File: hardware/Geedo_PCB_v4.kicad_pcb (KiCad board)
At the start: 2 copper layers, 29.5 x 51.5 mm, 23 parts, among them J1 USB-C, J2 BATTERY, J3 OLED, SW1 MAIN_BTN, SW2 BOOT_BTN, SW3 RESET_BTN, U1 MCP73831, U2 AMS1117-3.3, U3 ESP32-C3-MINI-1

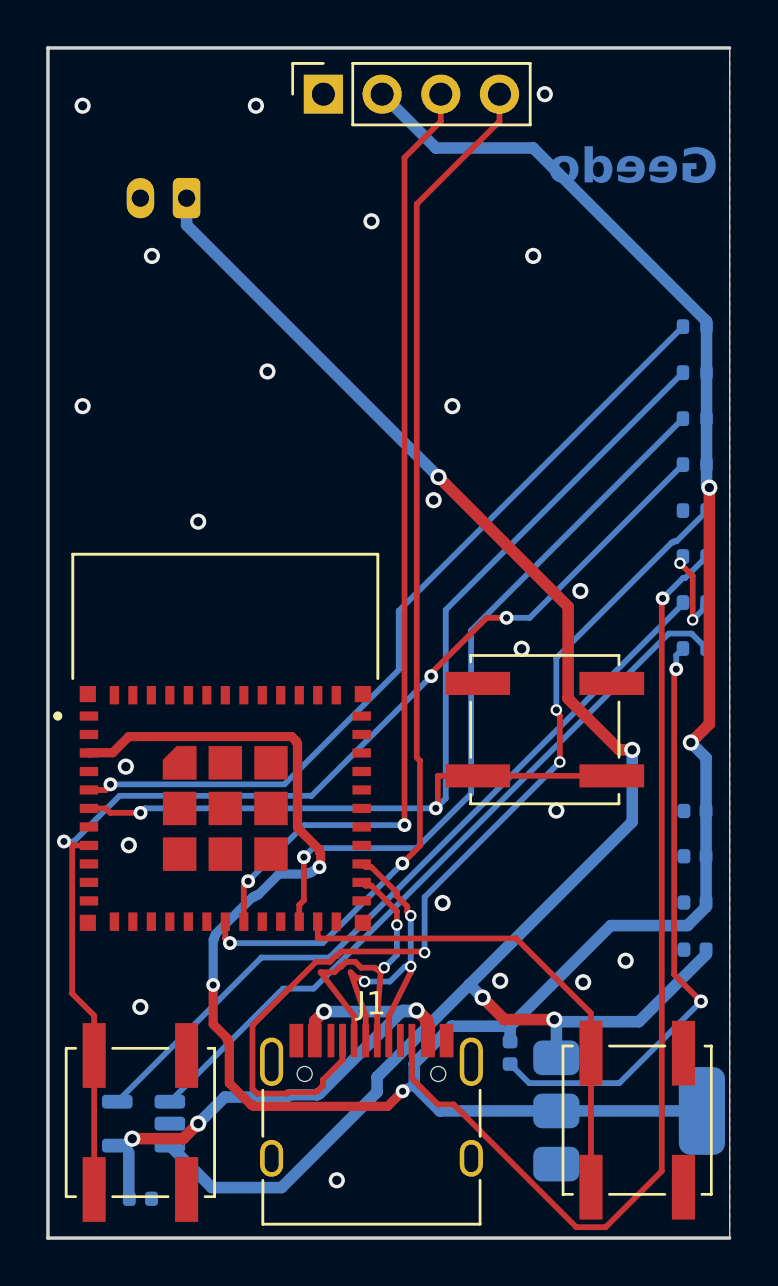
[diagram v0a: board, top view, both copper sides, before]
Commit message: hardware: replace AMS1117 with MCP1826S low-dropout regulator
The AMS1117 needs ~1.1 V of headroom, so on a LiPo it only holds 3.3 V near
full charge: at 3.7 V nominal the rail sits around 3.0 V, and an ESP32-C3's
300-400 mA WiFi transmit bursts widen the dropout further. The board would
have reset during WiFi at half battery - fatal for a robot that depends on
WiFi for updates and events.

MCP1826S-3302 drops 0.25 V and holds 3.3 V down to ~3.55 V of battery, using
the same SOT-223 footprint. It is not pin-compatible (AMS1117 is GND/Vout/Vin
with the tab on Vout; MCP1826S is Vin/GND/Vout with the tab on GND), so U2's
pads were remapped and VBAT/3V3 re-routed around it. The schematic symbol was
renumbered rather than redrawn, leaving every existing wire in place. The tab
now bonds to the ground pour, which also helps thermally.

Added C6, 1 uF on the back 2 mm from the output pin, as a local output
capacitor - C2's 10 uF sits 9 mm away. Its first position overlapped a 3V3
track and a VBAT via; the clearance audit caught both and it was moved to a
spot verified clear of every pad, track and via, with a gap even to same-net
pads.

Verified: schematic-to-board netlist 29/29 correct, every net except the
unfilled GND pour resolves to one island, and clearance is unchanged at the
9 pre-existing violations with none introduced.

Co-Authored-By: Claude Opus 5 <noreply@anthropic.com>
Claude-Session: https://claude.ai/code/session_011AnT632DFTLYxaJBrifUnG
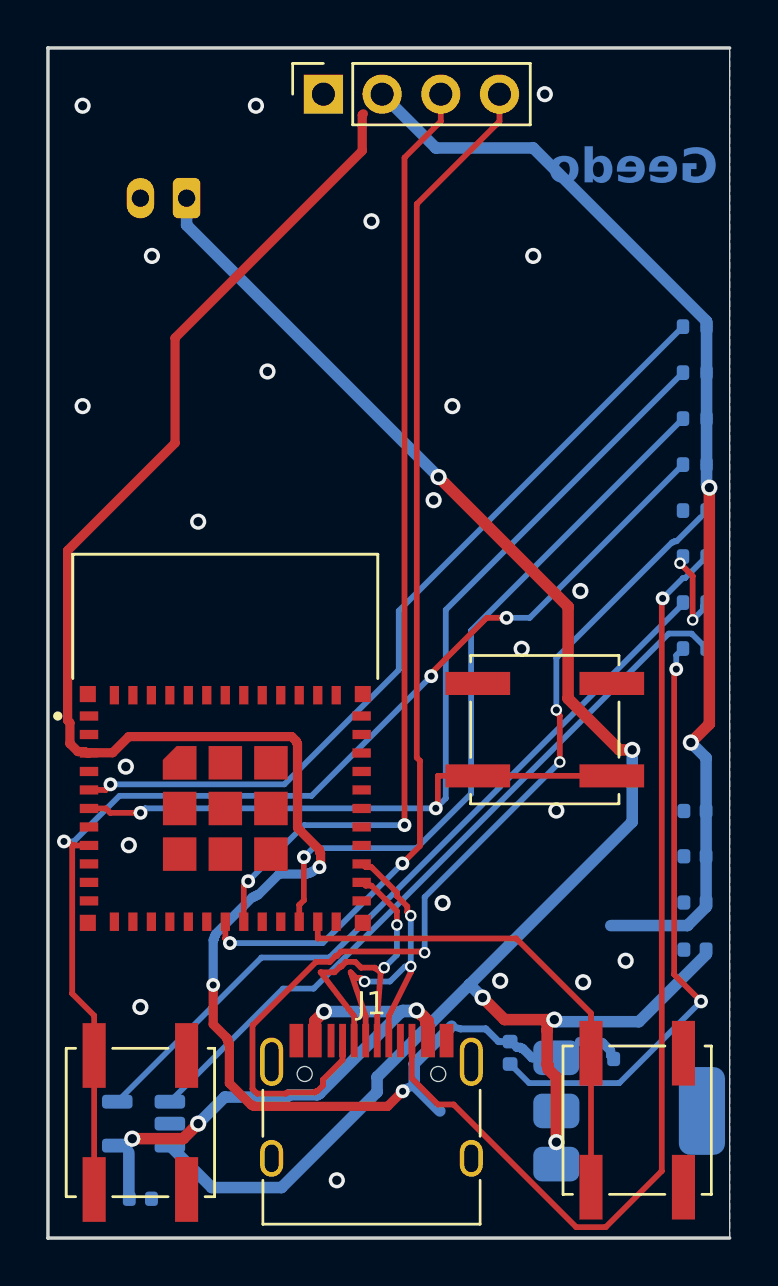
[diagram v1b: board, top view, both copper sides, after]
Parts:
- added C6: 1uF, Capacitor_SMD:C_0402_1005Metric, B.Cu at (113.5, 118.8)
- U2: value AMS1117-3.3 -> MCP1826S-3302
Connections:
- U2 pad 1: GND -> /VBAT
- U2 pad 2: +3V3 -> GND
- U2 pad 3: /VBAT -> +3V3
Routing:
- net +3V3: track 110.6 -> 130.2 mm
- net /VBAT: track 76.9 -> 81.7 mm, vias 4 -> 5

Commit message: hardware: add C7, the EN power-on reset capacitor
1 uF from EN to ground on the back, directly under the module's EN pad, 0.55 mm
from it. With R3's 10 k pull-up this forms the RC delay Espressif's design
guidelines call for: reset is held low while the 3.3 V rail rises, so the chip
starts cleanly on a slow power-up instead of occasionally hanging until the
reset button is pressed.

Two placement attempts were reverted before this one, both caught by the
verifiers rather than reaching the board:

- The first put the schematic symbol at coordinates crossed by the +3V3 bus
  wire at y=151.13, which merged EN into +3V3. The symbol now sits in space
  checked clear of every wire, symbol, label and junction.
- The second assumed pad 1 was the left-hand pad. The 0402 footprint is placed
  at rot 180, so pad 1 is on the right - meaning the ground pad landed where
  the EN pad was meant to go, shorting EN to ground and holding the chip in
  permanent reset. Placement is now computed from the footprint's real pad
  offsets and rotation, and tried at both orientations.

Verified after placing and again after routing: schematic-to-board netlist
29/29 correct, EN carries exactly U3.8, R3.2, SW3.1 and C7.1, and clearance is
unchanged at the 9 pre-existing violations with none introduced.

Co-Authored-By: Claude Opus 5 <noreply@anthropic.com>
Claude-Session: https://claude.ai/code/session_011AnT632DFTLYxaJBrifUnG
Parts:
- added C7: 1uF, Capacitor_SMD:C_0402_1005Metric, B.Cu at (91.5, 110.0)
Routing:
- net /EN_NET: track 50.1 -> 50.9 mm
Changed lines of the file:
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@@
 (footprint "Capacitor_SMD:C_0402_1005Metric"
 		(layer "B.Cu")
+		(at 91.5 110.0)
+		(descr "Capacitor SMD 0402 (1005 Metric), square (rectangular) end terminal, IPC_7351 nominal, (Body size source: IPC-SM-782 page 76, https://www.pcb-3d.com/wordpress/wp-content/uploads/ipc-sm-782a_amendment_1_and_2.pdf), generated with kicad-footprint-generator")
+		(tags "capacitor")
+		(property "Reference" "C7"
+			(at -17.79 -8.1 0)
+			(layer "B.SilkS")
+			(hide yes)
+			(effects
+				(font
+					(size 1 1)
+					(thickness 0.15)
+				)
+				(justify mirror)
+			)
+		)
+		(property "Value" "1uF"
+			(at 0 -1.16 0)
+			(layer "B.Fab")
+			(effects
+				(font
+					(size 1 1)
+					(thickness 0.15)
+				)
+				(justify mirror)
+			)
+		)
+		(property "Footprint" "Capacitor_SMD:C_0402_1005Metric"
+			(at 0 0 0)
+			(unlocked yes)
+			(layer "B.Fab")
+			(hide yes)
+			(effects
+				(font
+					(size 1.27 1.27)
+					(thickness 0.15)
+				)
+				(justify mirror)
+			)
+		)
+		(property "Datasheet" ""
+			(at 0 0 0)
+			(unlocked yes)
+			(layer "B.Fab")
+			(hide yes)
+			(effects
+				(font
+					(size 1.27 1.27)
+					(thickness 0.15)
+				)
+				(justify mirror)
+			)
+		)
+		(property "Description" ""
+			(at 0 0 0)
+			(unlocked yes)
+			(layer "B.Fab")
+			(hide yes)
+			(effects
+				(font
+					(size 1.27 1.27)
+					(thickness 0.15)
+				)
+				(justify mirror)
+			)
+		)
+		(sheetname "Root")
+		(sheetfile "Geedo_PCB_v4.kicad_sch")
+		(attr smd)
+		(fp_line
+			(start 0.107836 0.36)
+			(end -0.107836 0.36)
+			(stroke
+				(width 0.12)
+				(type solid)
+			)
+			(layer "B.SilkS")
+		)
+		(fp_line
+			(start 0.107836 -0.36)
+			(end -0.107836 -0.36)
+			(stroke
+				(width 0.12)
+				(type solid)
+			)
+			(layer "B.SilkS")
+		)
+		(fp_line
+			(start 0.91 0.46)
+			(end -0.91 0.46)
+			(stroke
+				(width 0.05)
+				(type solid)
+			)
+			(layer "B.CrtYd")
+		)
+		(fp_line
+			(start 0.91 -0.46)
+			(end 0.91 0.46)
+			(stroke
+				(width 0.05)
+				(type solid)
+			)
+			(layer "B.CrtYd")
+		)
+		(fp_line
+			(start -0.91 0.46)
+			(end -0.91 -0.46)
+			(stroke
+				(width 0.05)
+				(type solid)
+			)
+			(layer "B.CrtYd")
+		)
+		(fp_line
+			(start -0.91 -0.46)
+			(end 0.91 -0.46)
+			(stroke
+				(width 0.05)
+				(type solid)
+			)
+			(layer "B.CrtYd")
+		)
+		(fp_line
+			(start 0.5 0.25)
+			(end -0.5 0.25)
+			(stroke
+				(width 0.1)
+				(type solid)
+			)
+			(layer "B.Fab")
+		)
+		(fp_line
+			(start 0.5 -0.25)
+			(end 0.5 0.25)
+			(stroke
+				(width 0.1)
+				(type solid)
+			)
+			(layer "B.Fab")
+		)
+		(fp_line
+			(start -0.5 0.25)
+			(end -0.5 -0.25)
+			(stroke
+				(width 0.1)
+				(type solid)
+			)
+			(layer "B.Fab")
+		)
+		(fp_line
+			(start -0.5 -0.25)
+			(end 0.5 -0.25)
+			(stroke
+				(width 0.1)
+				(type solid)
+			)
+			(layer "B.Fab")
+		)
+		(fp_text user "${REFERENCE}"
+			(at 0 0 0)
+			(layer "B.Fab")
+			(effects
+				(font
+					(size 0.25 0.25)
+					(thickness 0.04)
+				)
+				(justify mirror)
+			)
+		)
+		(pad "1" smd roundrect
+			(at -0.48 0 180)
+			(size 0.56 0.62)
+			(layers "B.Cu" "B.Paste" "B.Mask")
+			(roundrect_rratio 0.25)
+			(net 10 "/EN_NET")
+			(pinfunction "1")
+			(pintype "passive")
+		)
+		(pad "2" smd roundrect
+			(at 0.48 0 180)
+			(size 0.56 0.62)
+			(layers "B.Cu" "B.Paste" "B.Mask")
+			(roundrect_rratio 0.25)
+			(net 2 "GND")
+			(pinfunction "2")
+			(pintype "passive")
+		)
+		(model "${KICAD8_3DMODEL_DIR}/Capacitor_SMD.3dshapes/C_0402_1005Metric.wrl"
+			(offset
+				(xyz 0 0 0)
+			)
+			(scale
+				(xyz 1 1 1)
+			)
+			(rotate
+				(xyz 0 0 0)
+			)
+		)
+	)
+(footprint "Capacitor_SMD:C_0402_1005Metric"
+		(layer "B.Cu")
 		(at 113.5 118.75 180)
 		(descr "Capacitor SMD 0402 (1005 Metric), square (rectangular) end terminal, IPC_7351 nominal, (Body size source: IPC-SM-782 page 76, https://www.pcb-3d.com/wordpress/wp-content/uploads/ipc-sm-782a_amendment_1_and_2.pdf), generated with kicad-footprint-generator")
@@
 		(net 3)
 	)
+	(segment
+		(start 91.02 110.0)
+		(end 91.0 110.0)
+		(width 0.25)
+		(layer "B.Cu")
+		(net 10)
+	)
+	(segment
+		(start 91.0 110.0)
+		(end 90.85 109.85)
+		(width 0.25)
+		(layer "B.Cu")
+		(net 10)
+	)
+	(segment
+		(start 90.85 109.85)
+		(end 90.85 109.65)
+		(width 0.25)
+		(layer "B.Cu")
+		(net 10)
+	)
+	(segment
+		(start 90.85 109.65)
+		(end 90.75 109.55)
+		(width 0.25)
+		(layer "B.Cu")
+		(net 10)
+	)
+	(segment
+		(start 90.75 109.55)
+		(end 90.62 109.338)
+		(width 0.25)
+		(layer "B.Cu")
+		(net 10)
+	)
 	(zone

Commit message: hardware: move MAIN button (SW1) 1.5 mm down
SW1 moves from (111, 104.5) to (111, 106). Board-only change - the
schematic is untouched.

The straight move failed two safety checks before a clean version landed,
each caught by the clearance gate and reverted rather than written:

- 1.5 mm down put SW1's ground pad on top of the VBAT trunk's F.Cu
  diagonal (0.25 mm overlap - a genuine short).
- Re-bending that diagonal into an L collided with CC1's descent, which
  owns the next 0.4 mm of that corner.

Final version: the VBAT diagonal is ripped and the maze router rebuilt the
bridge with the full obstacle model (9 copper items, dipping to the open
back layer), and the IO3 row tracks gained stubs following both button
pads to their new positions.

Gates after the change: clearance unchanged at the 9 pre-existing entries
(zero introduced), schematic-to-board netlist 29/29 consistent, IO3 and
VBAT each a single island. Zones ship unfilled as before - fill before DRC.

Co-Authored-By: Claude Fable 5 <noreply@anthropic.com>
Claude-Session: https://claude.ai/code/session_011AnT632DFTLYxaJBrifUnG
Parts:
- moved SW1 1.50 mm to (111.0, 106.0)
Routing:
- net /IO3: track 47.4 -> 50.4 mm
- net /VBAT: track 81.7 -> 83.7 mm, vias 5 -> 6
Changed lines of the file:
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@@
 	(footprint "Button_Switch_SMD:SW_Push_1P1T_NO_CK_KSC6xxJ"
 		(layer "F.Cu")
-		(at 111 104.5 180)
+		(at 111 106 180)
 		(descr "CK components KSC6 tactile switch https://www.ckswitches.com/media/1972/ksc6.pdf")
 		(tags "tactile switch ksc6")
@@
 	)
 	(segment
-		(start 112.0084 103.1569)
-		(end 114.2259 105.3744)
-		(width 0.5)
-		(layer "F.Cu")
-		(net 1)
-	)
-	(segment
 		(start 114.2259 105.3744)
 		(end 114.784 105.3744)
@@
 		(net 10)
 	)
+	(segment
+		(start 108.1 106.5)
+		(end 108.1 108.0)
+		(width 0.25)
+		(layer "F.Cu")
+		(net 8)
+	)
+	(segment
+		(start 113.9 106.5)
+		(end 113.9 108.0)
+		(width 0.25)
+		(layer "F.Cu")
+		(net 8)
+	)
+	(segment
+		(start 112.0 103.15)
+		(end 112.1 103.15)
+		(width 0.4)
+		(layer "F.Cu")
+		(net 1)
+	)
+	(segment
+		(start 112.1 103.15)
+		(end 112.15 103.1)
+		(width 0.4)
+		(layer "F.Cu")
+		(net 1)
+	)
+	(segment
+		(start 112.15 103.1)
+		(end 113.8 103.1)
+		(width 0.4)
+		(layer "F.Cu")
+		(net 1)
+	)
+	(segment
+		(start 113.8 103.1)
+		(end 113.9 103.0)
+		(width 0.4)
+		(layer "F.Cu")
+		(net 1)
+	)
+	(segment
+		(start 113.9 103.0)
+		(end 114.6 103.0)
+		(width 0.4)
+		(layer "F.Cu")
+		(net 1)
+	)
+	(segment
+		(start 114.6 103.0)
+		(end 114.6 104.9)
+		(width 0.4)
+		(layer "B.Cu")
+		(net 1)
+	)
+	(segment
+		(start 114.6 104.9)
+		(end 114.65 104.95)
+		(width 0.4)
+		(layer "B.Cu")
+		(net 1)
+	)
+	(segment
+		(start 114.65 104.95)
+		(end 114.784 105.374)
+		(width 0.4)
+		(layer "B.Cu")
+		(net 1)
+	)
+	(via
+		(at 114.6 103.0)
+		(size 0.6)
+		(drill 0.3)
+		(layers "F.Cu" "B.Cu")
+		(net 1)
+	)
 	(zone

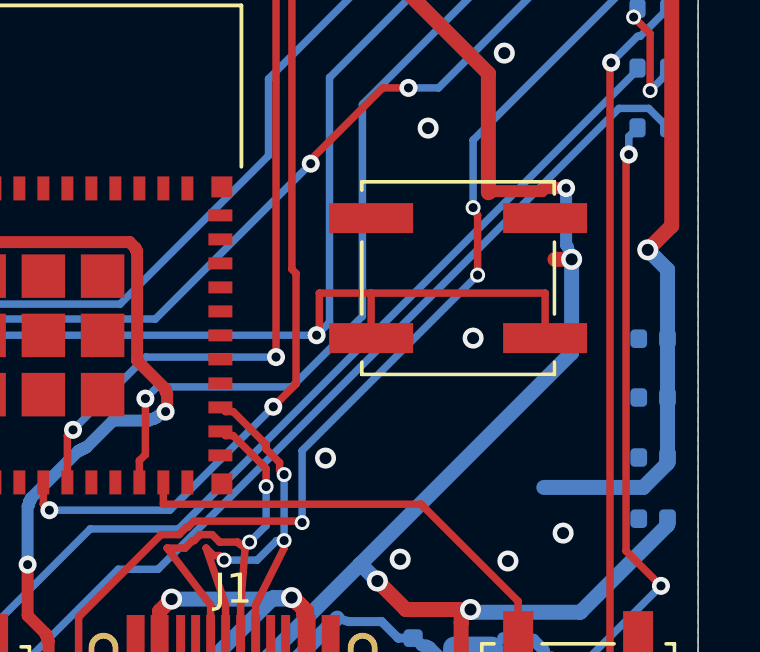
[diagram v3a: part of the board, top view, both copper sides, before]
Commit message: hardware: move MAIN button 3 mm further down
SW1 goes from (111, 106) to (111, 109) - 3 mm below where it sat, 4.5 mm
below its original position. Board-only; the schematic is untouched.

Two obstacles had to move out of the way first:

- The IO3 spur that fed the old pad row ran along y=106.5, exactly where
  the button's ground pads land now. Six segments were ripped and IO3 was
  rebuilt: a bar at y=111 joining both button pads, then a routed path
  back to the net. U3 and R1 stayed connected on the back layer throughout.
- The button's IO3 pad ended up 0.164 mm from a GND stitching via, 36 um
  short of the 0.2 mm rule. The via was one of the plane stitches and is
  free to move, so it shifted 0.1 mm rather than the button.

An intermediate position 1.5 mm higher was tried first and rejected: it put
the ground pad on top of the VBAT via and its track, two real shorts.

Gates after the change, against the pre-move baseline: clearance unchanged
at the 9 pre-existing entries with none introduced, edge 5, keepout 0,
schematic-to-board netlist 29/29 consistent, IO3 a single island.

Co-Authored-By: Claude Opus 5 <noreply@anthropic.com>
Claude-Session: https://claude.ai/code/session_011AnT632DFTLYxaJBrifUnG
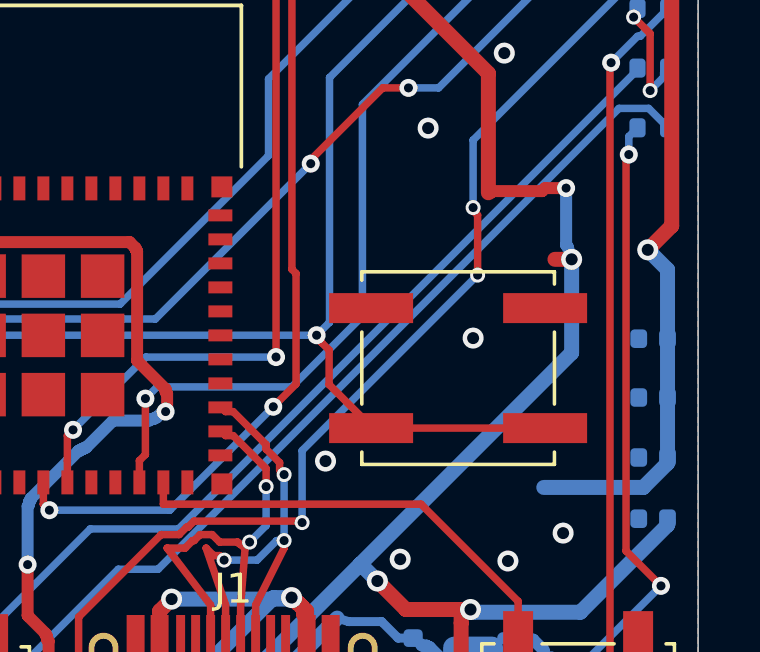
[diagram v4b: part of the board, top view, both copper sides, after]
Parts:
- moved SW1 3.00 mm to (111.0, 109.0)
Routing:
- net /IO3: track 50.4 -> 48.1 mm
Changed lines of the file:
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@@
 	(footprint "Button_Switch_SMD:SW_Push_1P1T_NO_CK_KSC6xxJ"
 		(layer "F.Cu")
-		(at 111 106 180)
+		(at 111 109 180)
 		(descr "CK components KSC6 tactile switch https://www.ckswitches.com/media/1972/ksc6.pdf")
 		(tags "tactile switch ksc6")
@@
 	)
 	(via
-		(at 106.58 112)
+		(at 106.58 112.1)
 		(size 0.7)
 		(drill 0.4)
@@
 	)
 	(segment
-		(start 106.2838 107.9041)
-		(end 106.3733 107.8146)
-		(width 0.25)
-		(layer "F.Cu")
-		(net 8)
-	)
-	(segment
 		(start 93.5066 108.0996)
 		(end 92.1913 108.0996)
@@
 	)
 	(segment
-		(start 106.3733 107.8146)
-		(end 106.3733 106.5)
-		(width 0.25)
-		(layer "F.Cu")
-		(net 8)
-	)
-	(segment
-		(start 108.1 106.5)
-		(end 106.3733 106.5)
-		(width 0.25)
-		(layer "F.Cu")
-		(net 8)
-	)
-	(segment
 		(start 92.1913 108.0996)
 		(end 92.0017 107.91)
@@
 		(net 8)
 	)
-	(segment
-		(start 108.1 106.5)
-		(end 113.9 106.5)
-		(width 0.25)
-		(layer "F.Cu")
-		(net 8)
-	)
 	(via
 		(at 93.5066 108.0996)
@@
 	)
 	(segment
-		(start 108.1 106.5)
-		(end 108.1 108.0)
-		(width 0.25)
-		(layer "F.Cu")
-		(net 8)
-	)
-	(segment
-		(start 113.9 106.5)
-		(end 113.9 108.0)
-		(width 0.25)
-		(layer "F.Cu")
-		(net 8)
-	)
-	(segment
 		(start 112.0 103.15)
 		(end 112.1 103.15)
@@
 		(net 1)
 	)
+	(segment
+		(start 108.1 111.0)
+		(end 113.9 111.0)
+		(width 0.25)
+		(layer "F.Cu")
+		(net 8)
+	)
+	(segment
+		(start 108.1 111.0)
+		(end 107.95 110.85)
+		(width 0.25)
+		(layer "F.Cu")
+		(net 8)
+	)
+	(segment
+		(start 107.95 110.85)
+		(end 107.95 110.8)
+		(width 0.25)
+		(layer "F.Cu")
+		(net 8)
+	)
+	(segment
+		(start 107.95 110.8)
+		(end 106.7 109.55)
+		(width 0.25)
+		(layer "F.Cu")
+		(net 8)
+	)
+	(segment
+		(start 106.7 109.55)
+		(end 106.7 108.4)
+		(width 0.25)
+		(layer "F.Cu")
+		(net 8)
+	)
+	(segment
+		(start 106.7 108.4)
+		(end 106.45 108.15)
+		(width 0.25)
+		(layer "F.Cu")
+		(net 8)
+	)
+	(segment
+		(start 106.45 108.15)
+		(end 106.284 107.904)
+		(width 0.25)
+		(layer "F.Cu")
+		(net 8)
+	)
 	(zone
